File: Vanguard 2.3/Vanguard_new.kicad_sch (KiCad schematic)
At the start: 83 parts, among them J1 USB_C_Receptacle_USB2.0_16P, J2 Conn_02x03_Pin, J3 Micro_SD_Card_Det1, J4 STARBOARD_SERVO, J5 PORTSIDE_SERVO, J6 Battery In, J7 EJECTION_SERVO, Q1 BSS138, Q2 BSS138, Q3 BSS138, Q4 BSS138, U1 ATSAMD11D14A-M, U2 ATmega4809-A, U3 AT25DF641A-SH-T, U4 AP2112K-3.3, U5 BD1020HFV, U6 BNO086, U7 TXB0104D, U8 TPS61092, U9 MPM3610AGQV-P, Y1 32.768kHz

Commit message: wiring, fiverr, etc
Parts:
- added BZ1: Buzzer, Buzzer_Beeper:MagneticBuzzer_Kingstate_KCG0601, symbol Device:Buzzer
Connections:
- net GND: now also BZ1.2 (-)
- net at Q4.3 (D): now also BZ1.1 (+)
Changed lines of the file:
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@@
 	(wire
 		(pts
-			(xy 391.16 104.14) (xy 391.16 109.22)
+			(xy 391.16 107.95) (xy 391.16 109.22)
 		)
 		(stroke
@@
 	)
 	(symbol
+		(lib_id "Device:Buzzer")
+		(at 393.7 105.41 90)
+		(unit 1)
+		(exclude_from_sim no)
+		(in_bom yes)
+		(on_board yes)
+		(dnp no)
+		(fields_autoplaced yes)
+		(property "Reference" "BZ1"
+			(at 397.51 103.3848 90)
+			(effects
+				(font
+					(size 1.27 1.27)
+				)
+				(justify right)
+			)
+		)
+		(property "Value" "Buzzer"
+			(at 397.51 105.9248 90)
+			(effects
+				(font
+					(size 1.27 1.27)
+				)
+				(justify right)
+			)
+		)
+		(property "Footprint" "Buzzer_Beeper:MagneticBuzzer_Kingstate_KCG0601"
+			(at 391.16 106.045 90)
+			(effects
+				(font
+					(size 1.27 1.27)
+				)
+				(hide yes)
+			)
+		)
+		(property "Datasheet" "~"
+			(at 391.16 106.045 90)
+			(effects
+				(font
+					(size 1.27 1.27)
+				)
+				(hide yes)
+			)
+		)
+		(property "Description" "Buzzer, polarized"
+			(at 393.7 105.41 0)
+			(effects
+				(font
+					(size 1.27 1.27)
+				)
+				(hide yes)
+			)
+		)
+		(pin "1"
+		)
+		(pin "2"
+		)
+		(instances
+			(project ""
+				(path "/972fbf12-2dcd-4fdf-b1c9-8a2880c46640"
+					(reference "BZ1")
+					(unit 1)
+				)
+			)
+		)
+	)
+	(symbol
 		(lib_id "Device:R")
 		(at 153.67 158.75 90)
@@
 	)
 	(symbol
-		(lib_id "power:+5V")
-		(at 386.08 104.14 180)
-		(unit 1)
-		(exclude_from_sim no)
-		(in_bom yes)
-		(on_board yes)
-		(dnp no)
-		(fields_autoplaced yes)
-		(property "Reference" "#PWR071"
-			(at 386.08 100.33 0)
-			(effects
-				(font
-					(size 1.27 1.27)
-				)
-				(hide yes)
-			)
-		)
-		(property "Value" "+5V"
-			(at 386.0801 107.95 90)
-			(effects
-				(font
-					(size 1.27 1.27)
-				)
-				(justify left)
-			)
-		)
-		(property "Footprint" ""
-			(at 386.08 104.14 0)
-			(effects
-				(font
-					(size 1.27 1.27)
-				)
-				(hide yes)
-			)
-		)
-		(property "Datasheet" ""
-			(at 386.08 104.14 0)
-			(effects
-				(font
-					(size 1.27 1.27)
-				)
-				(hide yes)
-			)
-		)
-		(property "Description" "Power symbol creates a global label with name \"+5V\""
-			(at 386.08 104.14 0)
-			(effects
-				(font
-					(size 1.27 1.27)
-				)
-				(hide yes)
-			)
-		)
-		(pin "1"
-		)
-		(instances
-			(project "Vanguard_new"
-				(path "/972fbf12-2dcd-4fdf-b1c9-8a2880c46640"
-					(reference "#PWR071")
-					(unit 1)
-				)
-			)
-		)
-	)
-	(symbol
 		(lib_id "BNO086:BNO086")
 		(at 104.14 156.21 0)
@@
 					(unit 1)
 				)
+			)
+		)
+	)
+	(symbol
+		(lib_id "power:GND")
+		(at 396.24 107.95 0)
+		(unit 1)
+		(exclude_from_sim no)
+		(in_bom yes)
+		(on_board yes)
+		(dnp no)
+		(fields_autoplaced yes)
+		(property "Reference" "#PWR02"
+			(at 396.24 114.3 0)
+			(effects
+				(font
+					(size 1.27 1.27)
+				)
+				(hide yes)
+			)
+		)
+		(property "Value" "GND"
+			(at 396.24 113.03 0)
+			(effects
+				(font
+					(size 1.27 1.27)
+				)
+			)
+		)
+		(property "Footprint" ""
+			(at 396.24 107.95 0)
+			(effects
+				(font
+					(size 1.27 1.27)
+				)
+				(hide yes)
+			)
+		)
+		(property "Datasheet" ""
+			(at 396.24 107.95 0)
+			(effects
+				(font
+					(size 1.27 1.27)
+				)
+				(hide yes)
+			)
+		)
+		(property "Description" "Power symbol creates a global label with name \"GND\" , ground"
+			(at 396.24 107.95 0)
+			(effects
+				(font
+					(size 1.27 1.27)
+				)
+				(hide yes)
+			)
+		)
+		(pin "1"
+		)
+		(instances
+			(project ""
+				(path "/972fbf12-2dcd-4fdf-b1c9-8a2880c46640"
+					(reference "#PWR02")
+					(unit 1)
+				)

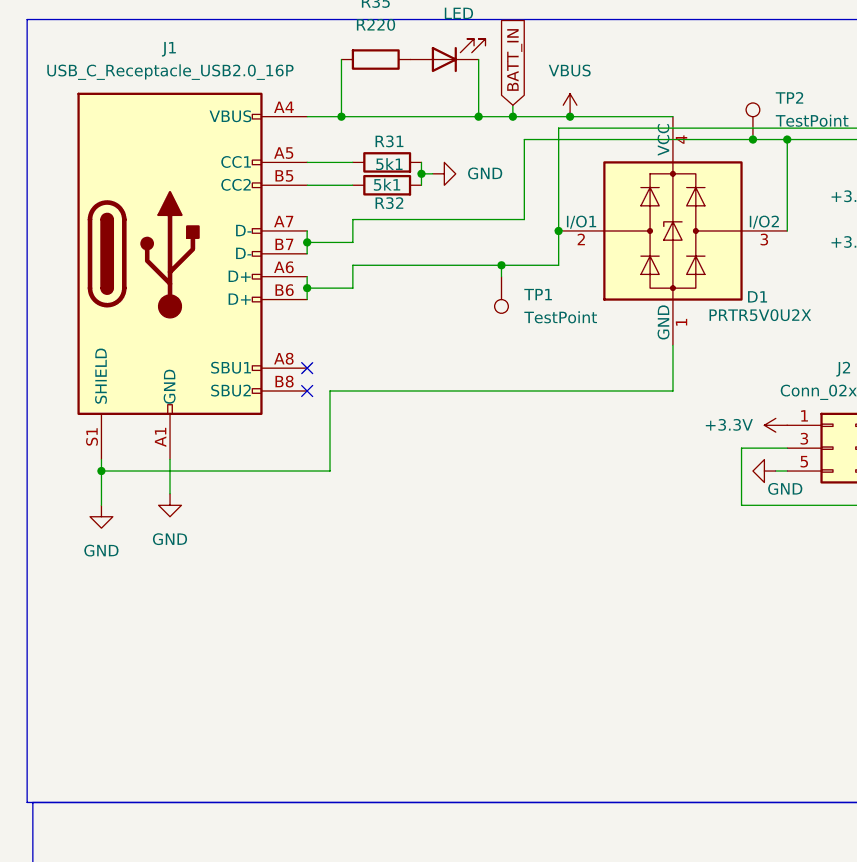
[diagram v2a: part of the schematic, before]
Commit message: added caps and reistor for emi and esd protection
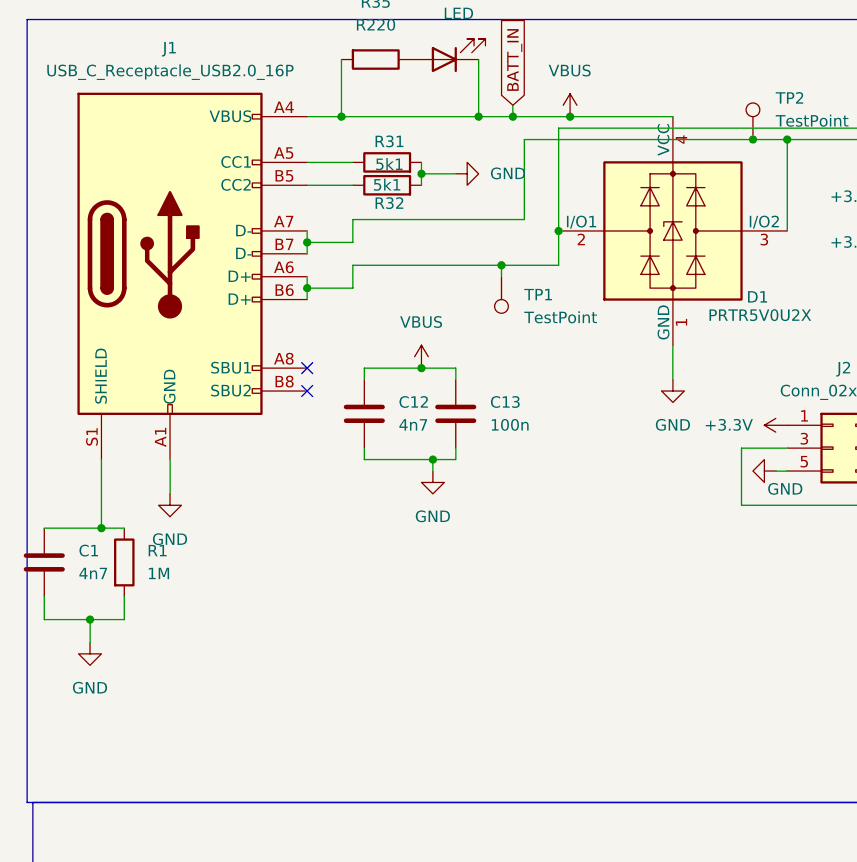
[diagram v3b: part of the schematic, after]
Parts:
- added C1, C12: 4n7, symbol Device:C
- added C13: 100n, symbol Device:C
- added R1: 1M, symbol Device:R
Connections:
- net GND: now also C1.2, C12.2, C13.2, R1.2; no longer J1.S1 (SHIELD)
- net VBUS: now also C12.1, C13.1
- new net: C1.1, J1.S1 (SHIELD), R1.1

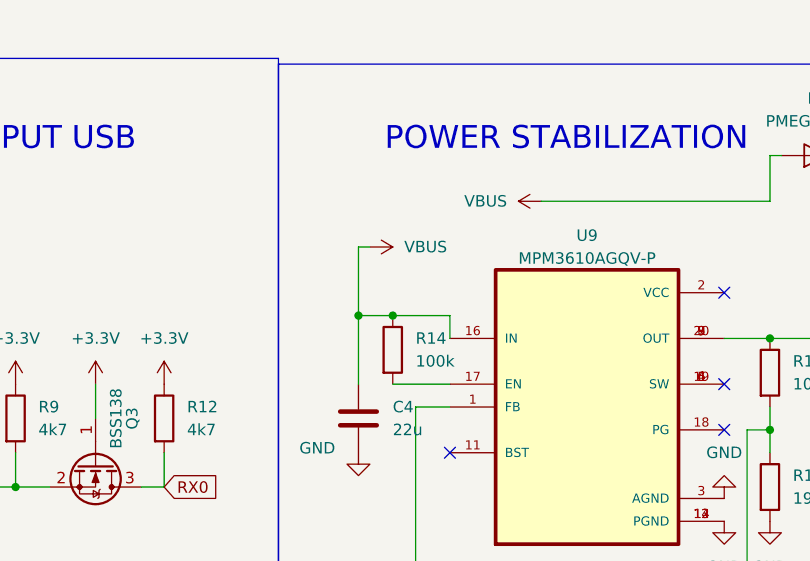
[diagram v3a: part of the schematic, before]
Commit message: removed a reductant vbus connection
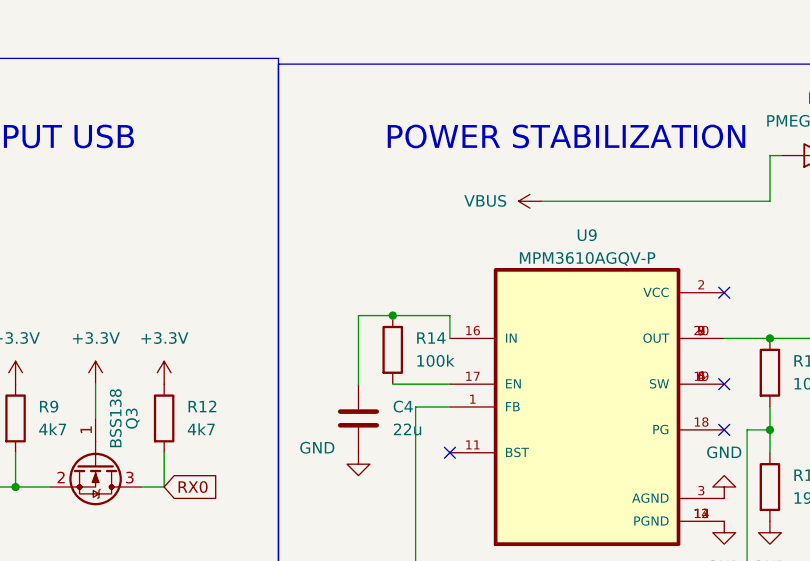
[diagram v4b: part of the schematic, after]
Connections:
- net VBUS: no longer C4.1, R14.1, U9.16 (IN)
- new net: C4.1, R14.1, U9.16 (IN)
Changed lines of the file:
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@@
 	)
 	(junction
-		(at 278.13 41.91)
-		(diameter 0)
-		(color 0 0 0 0)
-	)
-	(junction
 		(at 43.18 38.1)
 		(diameter 0)
@@
 	(wire
 		(pts
-			(xy 278.13 34.29) (xy 278.13 41.91)
-		)
-		(stroke
-			(width 0)
-			(type default)
-		)
-	)
-	(wire
-		(pts
 			(xy 374.65 114.3) (xy 377.19 114.3)
 		)
@@
 	(wire
 		(pts
-			(xy 279.4 34.29) (xy 278.13 34.29)
-		)
-		(stroke
-			(width 0)
-			(type default)
-		)
-	)
-	(wire
-		(pts
 			(xy 157.48 64.77) (xy 175.26 64.77)
 		)
@@
 					(unit 1)
 				)
-			)
-		)
-	)
-	(symbol
-		(lib_id "power:VBUS")
-		(at 279.4 34.29 270)
-		(unit 1)
-		(exclude_from_sim no)
-		(in_bom yes)
-		(on_board yes)
-		(dnp no)
-		(fields_autoplaced yes)
-		(property "Reference" "#PWR078"
-			(at 275.59 34.29 0)
-			(effects
-				(font
-					(size 1.27 1.27)
-				)
-				(hide yes)
-			)
-		)
-		(property "Value" "VBUS"
-			(at 283.21 34.2899 90)
-			(effects
-				(font
-					(size 1.27 1.27)
-				)
-				(justify left)
-			)
-		)
-		(property "Footprint" ""
-			(at 279.4 34.29 0)
-			(effects
-				(font
-					(size 1.27 1.27)
-				)
-				(hide yes)
-			)
-		)
-		(property "Datasheet" ""
-			(at 279.4 34.29 0)
-			(effects
-				(font
-					(size 1.27 1.27)
-				)
-				(hide yes)
-			)
-		)
-		(property "Description" "Power symbol creates a global label with name \"VBUS\""
-			(at 279.4 34.29 0)
-			(effects
-				(font
-					(size 1.27 1.27)
-				)
-				(hide yes)
-			)
-		)
-		(pin "1"
-		)
-		(instances
-			(project "Vanguard_new"
-				(path "/972fbf12-2dcd-4fdf-b1c9-8a2880c46640"
-					(reference "#PWR078")
-					(unit 1)
-				)

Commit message: kicad closed
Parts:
- removed C1: 4n7, symbol Device:C
- removed R1: 1M, symbol Device:R

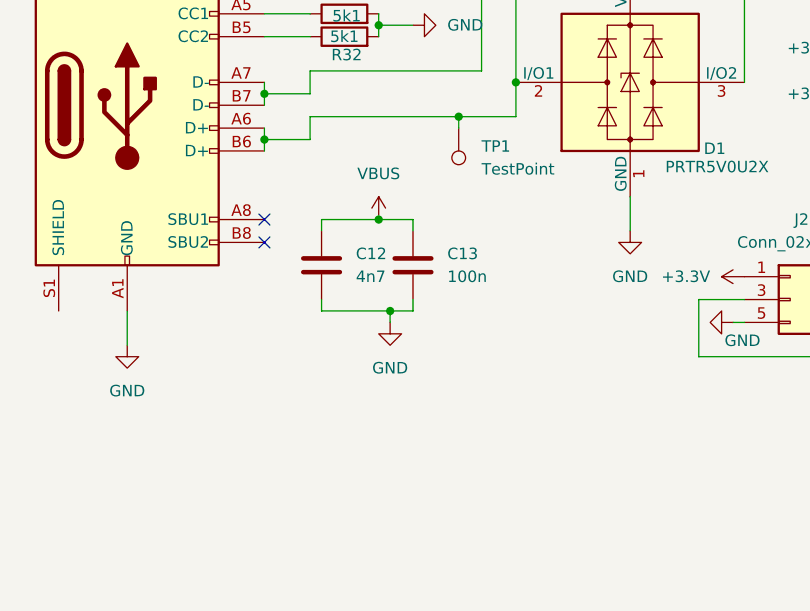
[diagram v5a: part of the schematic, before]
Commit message: missed gnd wiring
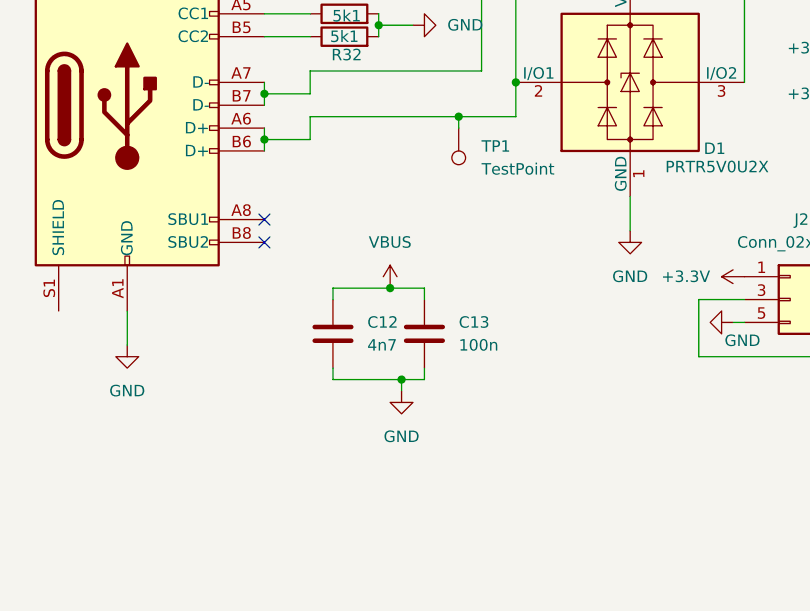
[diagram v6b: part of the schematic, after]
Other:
- moved on the sheet: C12, C13
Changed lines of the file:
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@@
 	)
 	(junction
-		(at 57.15 62.23)
+		(at 58.42 69.85)
 		(diameter 0)
 		(color 0 0 0 0)
@@
 	)
 	(junction
-		(at 55.88 52.07)
+		(at 57.15 59.69)
 		(diameter 0)
 		(color 0 0 0 0)
@@
 	(wire
 		(pts
-			(xy 49.53 62.23) (xy 57.15 62.23)
+			(xy 50.8 69.85) (xy 58.42 69.85)
 		)
 		(stroke
@@
 	(wire
 		(pts
-			(xy 55.88 52.07) (xy 59.69 52.07)
+			(xy 57.15 59.69) (xy 60.96 59.69)
 		)
 		(stroke
@@
 	(wire
 		(pts
-			(xy 59.69 62.23) (xy 59.69 60.96)
+			(xy 60.96 69.85) (xy 60.96 68.58)
 		)
 		(stroke
@@
 	(wire
 		(pts
-			(xy 49.53 53.34) (xy 49.53 52.07)
+			(xy 50.8 60.96) (xy 50.8 59.69)
 		)
 		(stroke
@@
 	(wire
 		(pts
-			(xy 57.15 62.23) (xy 59.69 62.23)
+			(xy 58.42 69.85) (xy 60.96 69.85)
 		)
 		(stroke
@@
 	(wire
 		(pts
-			(xy 49.53 60.96) (xy 49.53 62.23)
+			(xy 50.8 68.58) (xy 50.8 69.85)
 		)
 		(stroke
@@
 	(wire
 		(pts
-			(xy 49.53 52.07) (xy 55.88 52.07)
+			(xy 50.8 59.69) (xy 57.15 59.69)
 		)
 		(stroke
@@
 	(wire
 		(pts
-			(xy 59.69 52.07) (xy 59.69 53.34)
+			(xy 60.96 59.69) (xy 60.96 60.96)
 		)
 		(stroke
@@
 	(wire
 		(pts
-			(xy 57.15 62.23) (xy 57.15 63.5)
+			(xy 58.42 69.85) (xy 58.42 71.12)
 		)
 		(stroke
@@
 	(symbol
 		(lib_id "power:VBUS")
-		(at 55.88 52.07 0)
+		(at 57.15 59.69 0)
 		(unit 1)
 		(exclude_from_sim no)
@@
 		(fields_autoplaced yes)
 		(property "Reference" "#PWR071"
-			(at 55.88 55.88 0)
+			(at 57.15 63.5 0)
 			(effects
 				(font
@@
 		)
 		(property "Value" "VBUS"
-			(at 55.88 46.99 0)
+			(at 57.15 54.61 0)
 			(effects
 				(font
@@
 		)
 		(property "Footprint" ""
-			(at 55.88 52.07 0)
+			(at 57.15 59.69 0)
 			(effects
 				(font
@@
 		)
 		(property "Datasheet" ""
-			(at 55.88 52.07 0)
+			(at 57.15 59.69 0)
 			(effects
 				(font
@@
 		)
 		(property "Description" "Power symbol creates a global label with name \"VBUS\""
-			(at 55.88 52.07 0)
+			(at 57.15 59.69 0)
 			(effects
 				(font
@@
 	(symbol
 		(lib_id "power:GND")
-		(at 57.15 63.5 0)
+		(at 58.42 71.12 0)
 		(unit 1)
 		(exclude_from_sim no)
@@
 		(fields_autoplaced yes)
 		(property "Reference" "#PWR080"
-			(at 57.15 69.85 0)
+			(at 58.42 77.47 0)
 			(effects
 				(font
@@
 		)
 		(property "Value" "GND"
-			(at 57.15 68.58 0)
+			(at 58.42 76.2 0)
 			(effects
 				(font
@@
 		)
 		(property "Footprint" ""
-			(at 57.15 63.5 0)
+			(at 58.42 71.12 0)
 			(effects
 				(font
@@
 		)
 		(property "Datasheet" ""
-			(at 57.15 63.5 0)
+			(at 58.42 71.12 0)
 			(effects
 				(font
@@
 		)
 		(property "Description" "Power symbol creates a global label with name \"GND\" , ground"
-			(at 57.15 63.5 0)
+			(at 58.42 71.12 0)
 			(effects
 				(font
@@
 	(symbol
 		(lib_id "Device:C")
-		(at 59.69 57.15 0)
+		(at 60.96 64.77 0)
 		(unit 1)
 		(exclude_from_sim no)
@@
 		(fields_autoplaced yes)
 		(property "Reference" "C13"
-			(at 63.5 55.8799 0)
+			(at 64.77 63.4999 0)
 			(effects
 				(font
@@
 		)
 		(property "Value" "100n"
-			(at 63.5 58.4199 0)
+			(at 64.77 66.0399 0)
 			(effects
 				(font
@@
 		)
 		(property "Footprint" ""
-			(at 60.6552 60.96 0)
+			(at 61.9252 68.58 0)
 			(effects
 				(font
@@
 		)
 		(property "Datasheet" "~"
-			(at 59.69 57.15 0)
+			(at 60.96 64.77 0)
 			(effects
 				(font
@@
 		)
 		(property "Description" "Unpolarized capacitor"
-			(at 59.69 57.15 0)
+			(at 60.96 64.77 0)
 			(effects
 				(font
@@
 	(symbol
 		(lib_id "Device:C")
-		(at 49.53 57.15 0)
+		(at 50.8 64.77 0)
 		(unit 1)
 		(exclude_from_sim no)
@@
 		(on_board yes)
 		(dnp no)
-		(fields_autoplaced yes)
 		(property "Reference" "C12"
-			(at 53.34 55.8799 0)
+			(at 54.61 63.4999 0)
 			(effects
 				(font
@@
 		)
 		(property "Value" "4n7"
-			(at 53.34 58.4199 0)
+			(at 54.61 66.0399 0)
 			(effects
 				(font
@@
 		)
 		(property "Footprint" ""
-			(at 50.4952 60.96 0)
+			(at 51.7652 68.58 0)
 			(effects
 				(font
@@
 		)
 		(property "Datasheet" "~"
-			(at 49.53 57.15 0)
+			(at 50.8 64.77 0)
 			(effects
 				(font
@@
 		)
 		(property "Description" "Unpolarized capacitor"
-			(at 49.53 57.15 0)
+			(at 50.8 64.77 0)
 			(effects
 				(font

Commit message: ran drc and assign footprints
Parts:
- C12, C13: footprint (none) -> Capacitor_SMD:C_0201_0603Metric
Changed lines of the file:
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@@
 			)
 		)
-		(property "Footprint" ""
+		(property "Footprint" "Capacitor_SMD:C_0201_0603Metric"
 			(at 61.9252 68.58 0)
 			(effects
@@
 			)
 		)
-		(property "Footprint" ""
+		(property "Footprint" "Capacitor_SMD:C_0201_0603Metric"
 			(at 51.7652 68.58 0)
 			(effects

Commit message: ran sch parity test and assigned a footprint for U9
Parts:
- U9: footprint Package_DFN_QFN:QFN-16-1EP_3x3mm_P0.5mm_EP1.7x1.7mm -> Package_DFN_QFN:QFN-20-1EP_4x4mm_P0.5mm_EP2.5x2.5mm_ThermalVias
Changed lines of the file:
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@@
 			)
 		)
-		(property "Footprint" "Package_DFN_QFN:QFN-16-1EP_3x3mm_P0.5mm_EP1.7x1.7mm"
+		(property "Footprint" "Package_DFN_QFN:QFN-20-1EP_4x4mm_P0.5mm_EP2.5x2.5mm_ThermalVias"
 			(at 303.53 52.07 0)
 			(effects
